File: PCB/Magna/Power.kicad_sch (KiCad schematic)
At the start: 43 parts, among them U901 TPS61040DBV, U902 XL1509-ADJ, U903 WS3222D, U904 AMS1117-5.0, U905 AP2171W

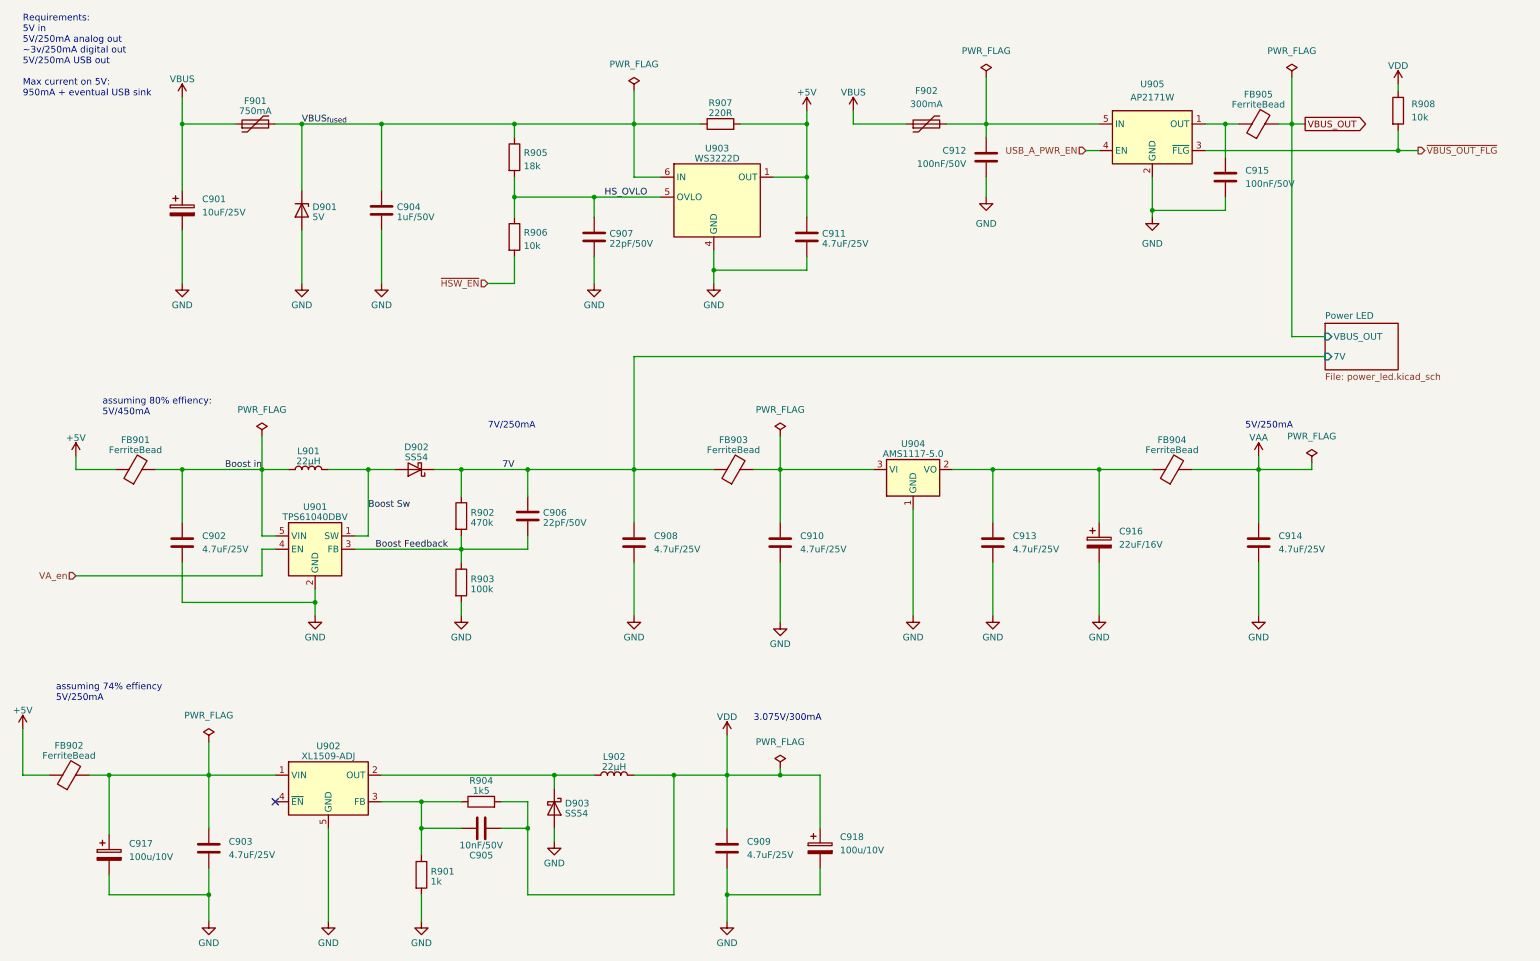
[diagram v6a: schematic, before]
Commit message: Split schematic to several projects
To allow for several boards to be done a kicad project
is needed for each
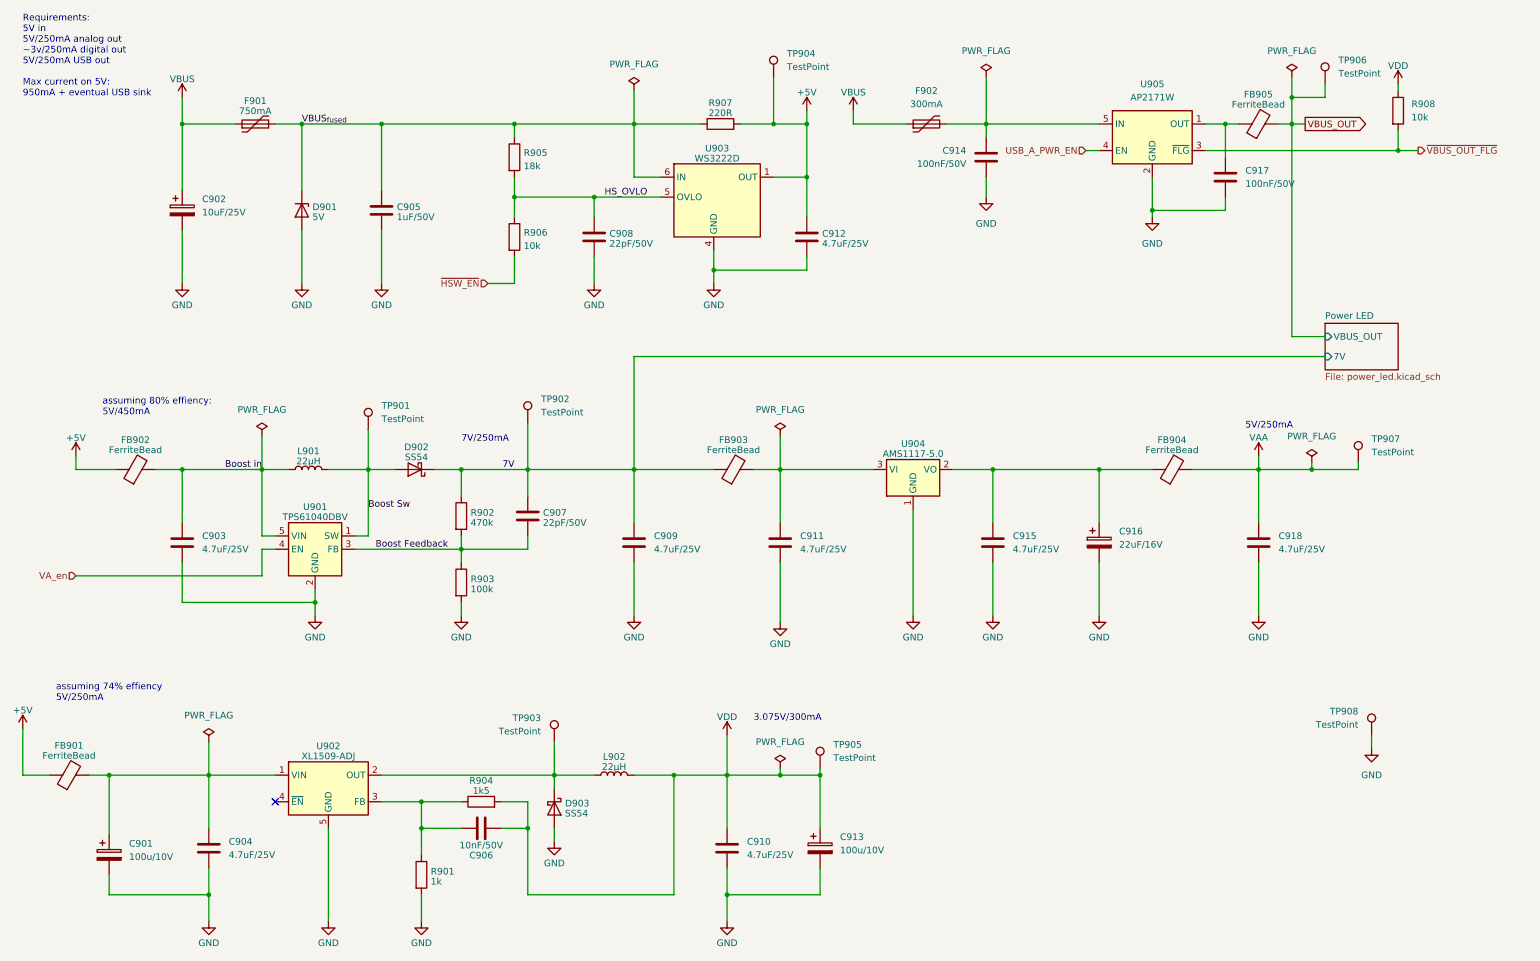
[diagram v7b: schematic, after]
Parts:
- added TP901, TP902, TP903, TP904, TP905, TP906, TP907, TP908: TestPoint, TestPoint:TestPoint_Keystone_5005-5009_Compact, symbol Connector:TestPoint
- renumbered C917 to C901, C901 to C902, C902 to C903, C903 to C904, C904 to C905, C905 to C906, C906 to C907, C907 to C908, C908 to C909, C909 to C910, C910 to C911, C911 to C912, C918 to C913, C912 to C914, C913 to C915, C915 to C917, C914 to C918, FB902 to FB901, FB901 to FB902
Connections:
- net +5V: now also TP904.1
- net 7V: now also TP902.1
- net Boost Sw: now also TP901.1
- net GND: now also TP908.1
- net VAA: now also TP907.1
- net VBUS_OUT: now also TP906.1
- net VDD: now also TP905.1
- net at D903.1 (K), L902.1, U902.2 (OUT): now also TP903.1

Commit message: Move VAA circuitry to Analogue daughterboard (#11)
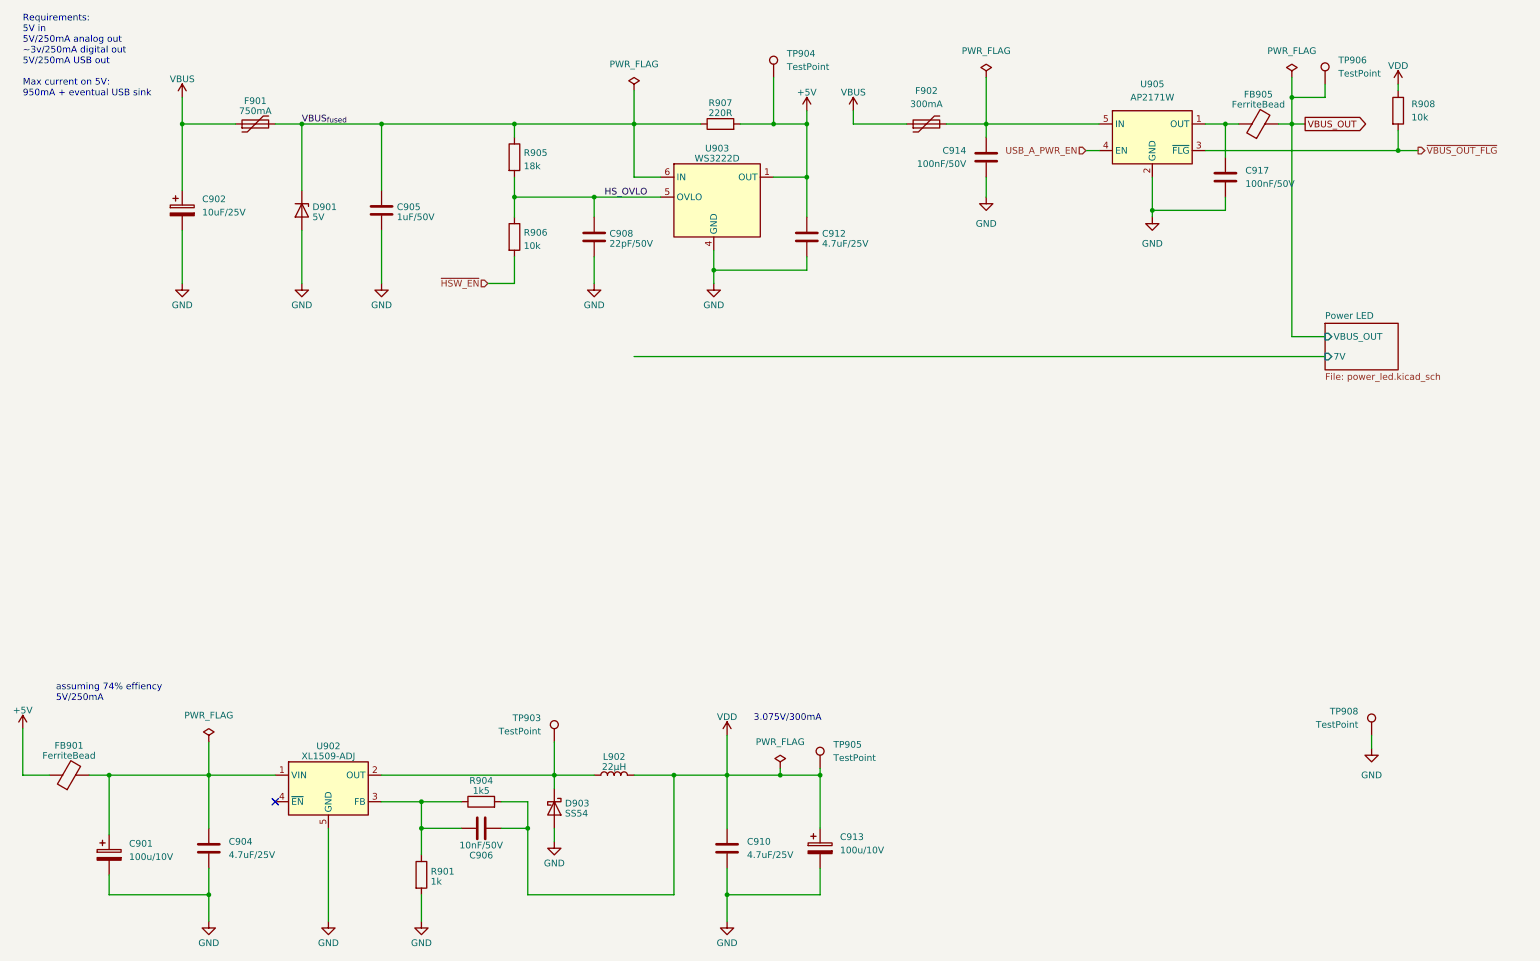
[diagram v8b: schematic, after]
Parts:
- removed C903, C909, C911, C915, C918: 4.7uF/25V, Capacitor_SMD:C_0805_2012Metric_Pad1.18x1.45mm_HandSolder, symbol Device:C
- removed C907: 22pF/50V, Capacitor_SMD:C_0805_2012Metric_Pad1.18x1.45mm_HandSolder, symbol Device:C
- removed C916: 22uF/16V, Capacitor_SMD:CP_Elec_5x5.8, symbol Device:C_Polarized
- removed D902: SS54, Diode_SMD:D_SMA_Handsoldering, symbol Device:D_Schottky
- removed FB902, FB903, FB904: FerriteBead, Inductor_SMD:L_0805_2012Metric, symbol Device:FerriteBead
- removed L901: 22µH, Skrooter_footprints:MSCD43, symbol Device:L
- removed R902: 470k, Resistor_SMD:R_0805_2012Metric_Pad1.20x1.40mm_HandSolder, symbol Device:R
- removed R903: 100k, Resistor_SMD:R_0805_2012Metric_Pad1.20x1.40mm_HandSolder, symbol Device:R
- removed TP901, TP902, TP907: TestPoint, TestPoint:TestPoint_Keystone_5005-5009_Compact, symbol Connector:TestPoint
- removed U901: TPS61040DBV, Package_TO_SOT_SMD:SOT-23-5, symbol Regulator_Switching:TPS61040DBV
- removed U904: AMS1117-5.0, Package_TO_SOT_SMD:SOT-223-3_TabPin2, symbol Regulator_Linear:AMS1117-5.0
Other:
- note removed: "5V/250mA"
- note removed: "7V/250mA"
- note removed: "assuming 80% effiency: 5V/450mA"
